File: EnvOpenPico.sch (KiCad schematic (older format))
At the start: 38 parts, among them J2 B3U-1000P, J3 2.54mm header 01x20, J4 2.54mm header 01x20, J5 Conn_01x03_Male, U1 RT6150B-33GQW, U3 RP2040, X1 XO 32 12Mhz 3225 seiko

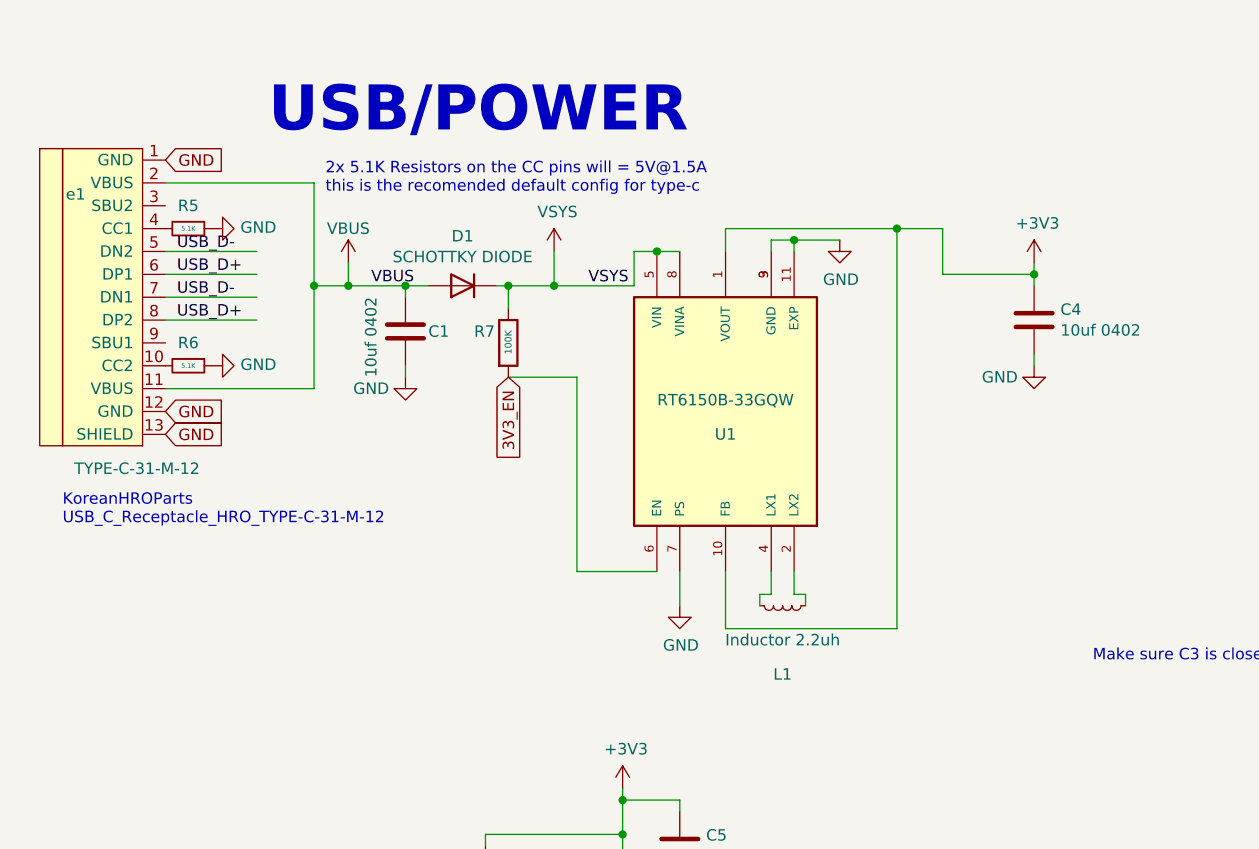
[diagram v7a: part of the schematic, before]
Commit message: Swapped RT6150GQW for TPS63002
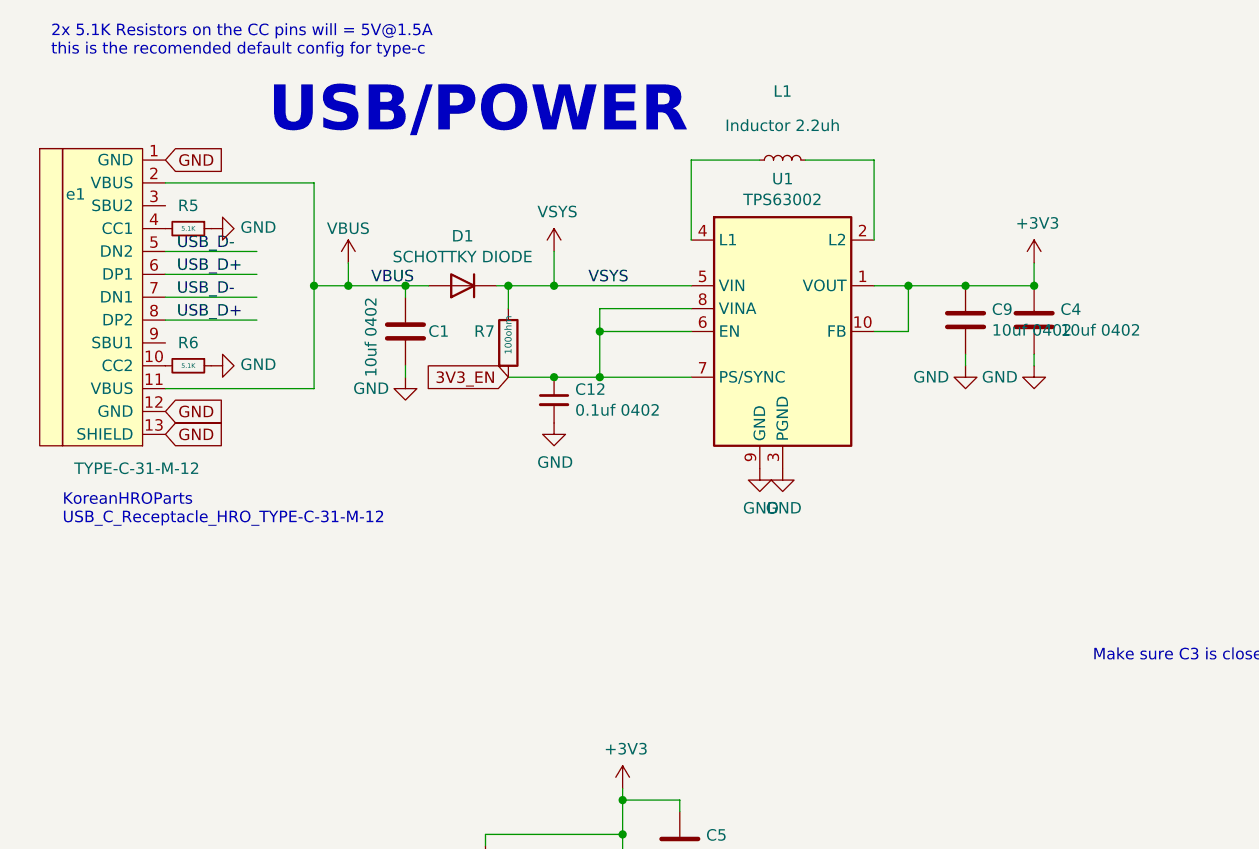
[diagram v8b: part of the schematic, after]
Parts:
- removed U1: RT6150B-33GQW, RT6150B-33GQW:SON50P250X250X80-11N, symbol RT6150B-33GQW:RT6150B-33GQW
- added C12: 0.1uf 0402, Capacitor_SMD:C_0402_1005Metric, symbol Device:C_Small
- added C9: 10uf 0402, Capacitor_SMD:C_0402_1005Metric, symbol Device:C
- added U1: TPS63002, Package_SON:Texas_DRC0010J_ThermalVias, symbol Regulator_Switching:TPS63002
- R7: value 100K -> 100ohm
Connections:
- net +3V3: now also C9.1, U1.1 (VOUT), U1.10 (FB)
- net 3V3_EN: now also C12.1, U1.6 (EN), U1.7 (PS/SYNC), U1.8 (VINA)
- net GND: now also C12.2, C9.2, U1.11 (PGND), U1.3 (PGND), U1.9 (GND)
- net VBUS: now also U1.5 (VIN)
- net at L1.1: now also U1.4 (L1)
- net at L1.2: now also U1.2 (L2)
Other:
- moved on the sheet: L1
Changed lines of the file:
@@
 	1    0    0    -1
 $EndComp
-Wire Wire Line
-	4500 1700 4900 1700
-Wire Wire Line
-	4900 1700 4900 1650
 $Comp
 L power:+3V3 #PWR09
@@
 Wire Wire Line
 	4900 2050 4900 2100
-Wire Wire Line
-	4900 1750 4900 1700
-Connection ~ 4900 1700
 Wire Wire Line
 	8450 3000 8800 3000
@@
 Text Notes 9300 2350 0    50   ~ 0
 These decoupling capacitors are meant\nto be put close by each 3.3V pin of the RP2040
-Text Notes 1800 1350 0    50   ~ 0
+Text Notes 600  750  0    50   ~ 0
 2x 5.1K Resistors on the CC pins will = 5V@1.5A\nthis is the recomended default config for type-c
-Text GLabel 2600 2150 3    50   Input ~ 0
+Text GLabel 2600 2150 0    50   Input ~ 0
 3V3_EN
 $Comp
@@
 P 2600 2000
 F 0 "R7" H 2450 2050 50  0000 L CNN
-F 1 "100K" V 2600 1950 30  0000 L CNN
+F 1 "100ohm" V 2600 1950 30  0000 L CNN
 F 2 "Resistor_SMD:R_0402_1005Metric" V 2530 2000 50  0001 C CNN
 F 3 "" H 2600 2000 50  0001 C CNN
@@
 	2600 1850 2600 1750
 $Comp
-L RT6150B-33GQW:RT6150B-33GQW U1
-U 1 1 60C00F4F
-P 3550 2300
-F 0 "U1" V 3450 2300 50  0000 C CNN
-F 1 "RT6150B-33GQW" V 3600 2300 50  0000 C CNN
-F 2 "RT6150B-33GQW:SON50P250X250X80-11N" H 3550 2300 50  0001 L BNN
-F 3 "" H 3550 2300 50  0001 L BNN
-F 4 "Richtek" H 3550 2300 50  0001 L BNN "MANUFACTURER"
-	1    3550 2300
-	0    -1   -1   0
-$EndComp
-Wire Wire Line
-	3350 1600 3250 1600
-Connection ~ 3250 1600
-Wire Wire Line
-	3550 1600 3550 1500
-Wire Wire Line
-	4500 1500 4500 1700
-Wire Wire Line
-	3750 1600 3750 1550
-Wire Wire Line
-	3750 1550 3850 1550
-Wire Wire Line
-	3850 1550 3850 1600
-Wire Wire Line
-	3850 1550 4050 1550
-Connection ~ 3850 1550
-$Comp
 L power:GND #PWR0110
 U 1 1 60C62E0C
-P 4050 1550
-F 0 "#PWR0110" H 4050 1300 50  0001 C CNN
-F 1 "GND" H 4055 1377 50  0000 C CNN
-F 2 "" H 4050 1550 50  0001 C CNN
-F 3 "" H 4050 1550 50  0001 C CNN
-	1    4050 1550
+P 3700 2550
+F 0 "#PWR0110" H 3700 2300 50  0001 C CNN
+F 1 "GND" H 3705 2377 50  0000 C CNN
+F 2 "" H 3700 2550 50  0001 C CNN
+F 3 "" H 3700 2550 50  0001 C CNN
+	1    3700 2550
 	1    0    0    -1
 $EndComp
 Wire Wire Line
 	1900 1650 1900 1750
-Wire Wire Line
-	2900 2150 2900 3000
-Wire Wire Line
-	2900 3000 3250 3000
-Wire Wire Line
-	2600 2150 2900 2150
-Wire Wire Line
-	3350 3000 3350 3150
 $Comp
 L power:GND #PWR0111
 U 1 1 60C8A405
-P 3350 3150
-F 0 "#PWR0111" H 3350 2900 50  0001 C CNN
-F 1 "GND" H 3355 2977 50  0000 C CNN
-F 2 "" H 3350 3150 50  0001 C CNN
-F 3 "" H 3350 3150 50  0001 C CNN
-	1    3350 3150
-	1    0    0    -1
-$EndComp
-Wire Wire Line
-	3550 3000 3550 3250
-Wire Wire Line
-	4300 3250 4300 1500
-Wire Wire Line
-	3550 1500 4300 1500
-Wire Wire Line
-	3550 3250 4300 3250
-Connection ~ 4300 1500
-Wire Wire Line
-	4300 1500 4500 1500
+P 2800 2350
+F 0 "#PWR0111" H 2800 2100 50  0001 C CNN
+F 1 "GND" H 2805 2177 50  0000 C CNN
+F 2 "" H 2800 2350 50  0001 C CNN
+F 3 "" H 2800 2350 50  0001 C CNN
+	1    2800 2350
+	1    0    0    -1
+$EndComp
 $Comp
 L Device:L_Small L1
 U 1 1 60C9C176
-P 3800 3150
-F 0 "L1" V 4100 3150 50  0000 C CNN
-F 1 "Inductor 2.2uh" V 3950 3150 50  0000 C CNN
-F 2 "Inductor_SMD:L_0805_2012Metric" H 3800 3150 50  0001 C CNN
-F 3 "~" H 3800 3150 50  0001 C CNN
-	1    3800 3150
-	0    1    1    0
-$EndComp
-Wire Wire Line
-	3850 3000 3850 3100
-Wire Wire Line
-	3850 3100 3900 3100
-Wire Wire Line
-	3900 3100 3900 3150
-Wire Wire Line
-	3700 3150 3700 3100
-Wire Wire Line
-	3700 3100 3750 3100
-Wire Wire Line
-	3750 3100 3750 3000
+P 3800 1200
+F 0 "L1" V 4100 1200 50  0000 C CNN
+F 1 "Inductor 2.2uh" V 3950 1200 50  0000 C CNN
+F 2 "Inductor_SMD:L_0805_2012Metric" H 3800 1200 50  0001 C CNN
+F 3 "~" H 3800 1200 50  0001 C CNN
+	1    3800 1200
+	0    -1   -1   0
+$EndComp
 $Comp
 L Simulation_SPICE:DIODE D1
@@
 Connection ~ 2600 1750
 Wire Wire Line
-	3150 1750 3150 1600
-Wire Wire Line
-	3150 1600 3250 1600
-Wire Wire Line
 	2600 1750 2800 1750
 Wire Wire Line
 	2800 1750 2800 1600
 Connection ~ 2800 1750
-Wire Wire Line
-	2800 1750 3150 1750
 $Comp
 L VSYS:VSYS #PWR0112
@@
 Text Label 2000 1750 0    50   ~ 0
 VBUS
+$Comp
+L Regulator_Switching:TPS63002 U1
+U 1 1 60D7C270
+P 3800 1950
+F 0 "U1" H 3800 2617 50  0000 C CNN
+F 1 "TPS63002" H 3800 2526 50  0000 C CNN
+F 2 "Package_SON:Texas_DRC0010J_ThermalVias" H 4650 1400 50  0001 C CNN
+F 3 "http://www.ti.com/lit/ds/symlink/tps63000.pdf" H 3500 2500 50  0001 C CNN
+	1    3800 1950
+	1    0    0    -1
+$EndComp
+Wire Wire Line
+	4900 1650 4900 1750
+Wire Wire Line
+	3400 1550 3400 1200
+Wire Wire Line
+	3400 1200 3700 1200
+Wire Wire Line
+	4200 1550 4200 1200
+Wire Wire Line
+	4200 1200 3900 1200
+Wire Wire Line
+	2800 1750 3400 1750
+Wire Wire Line
+	3000 2150 3000 1950
+Wire Wire Line
+	3000 1850 3400 1850
+Wire Wire Line
+	2600 2150 2800 2150
+Wire Wire Line
+	3400 1950 3000 1950
+Connection ~ 3000 1950
+Wire Wire Line
+	3000 1950 3000 1850
+Wire Wire Line
+	3400 2150 3000 2150
+Connection ~ 3000 2150
+$Comp
+L Device:C_Small C12
+U 1 1 60E73823
+P 2800 2250
+F 0 "C12" H 2892 2296 50  0000 L CNN
+F 1 "0.1uf 0402" H 2892 2205 50  0000 L CNN
+F 2 "Capacitor_SMD:C_0402_1005Metric" H 2800 2250 50  0001 C CNN
+F 3 "~" H 2800 2250 50  0001 C CNN
+	1    2800 2250
+	1    0    0    -1
+$EndComp
+Connection ~ 2800 2150
+Wire Wire Line
+	2800 2150 3000 2150
+$Comp
+L Device:C C9
+U 1 1 60E776B9
+P 4600 1900
+F 0 "C9" H 4715 1946 50  0000 L CNN
+F 1 "10uf 0402" H 4715 1855 50  0000 L CNN
+F 2 "Capacitor_SMD:C_0402_1005Metric" H 4638 1750 50  0001 C CNN
+F 3 "" H 4600 1900 50  0001 C CNN
+	1    4600 1900
+	1    0    0    -1
+$EndComp
+$Comp
+L power:GND #PWR01
+U 1 1 60E776BF
+P 4600 2100
+F 0 "#PWR01" H 4600 1850 50  0001 C CNN
+F 1 "GND" H 4450 2050 50  0000 C CNN
+F 2 "" H 4600 2100 50  0001 C CNN
+F 3 "" H 4600 2100 50  0001 C CNN
+	1    4600 2100
+	1    0    0    -1
+$EndComp
+Wire Wire Line
+	4600 2050 4600 2100
+Wire Wire Line
+	4900 1750 4600 1750
+Connection ~ 4900 1750
+Wire Wire Line
+	4200 1750 4350 1750
+Connection ~ 4600 1750
+Wire Wire Line
+	4200 1950 4350 1950
+Wire Wire Line
+	4350 1950 4350 1750
+Connection ~ 4350 1750
+Wire Wire Line
+	4350 1750 4600 1750
+$Comp
+L power:GND #PWR05
+U 1 1 60EAD68C
+P 3800 2550
+F 0 "#PWR05" H 3800 2300 50  0001 C CNN
+F 1 "GND" H 3805 2377 50  0000 C CNN
+F 2 "" H 3800 2550 50  0001 C CNN
+F 3 "" H 3800 2550 50  0001 C CNN
+	1    3800 2550
+	1    0    0    -1
+$EndComp
 $EndSCHEMATC
